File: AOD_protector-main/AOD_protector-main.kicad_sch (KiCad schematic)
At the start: 33 parts, among them IC1 MAX9141ESA+, J1 Input, J2 5V from source, J3 Output, J4 to fault handler, Q1 BSS316N, Q2 BSS316N, Q3 BSS316N, SW1 SW_Push, U1 REF35102QDBVR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

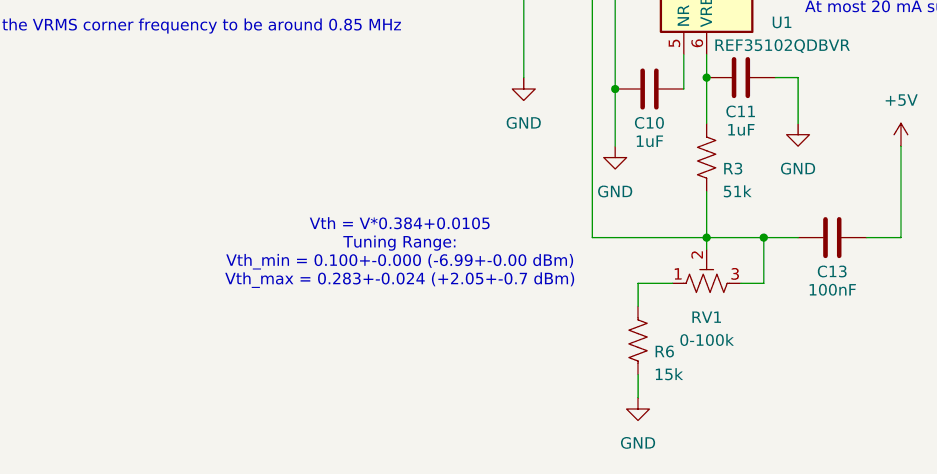
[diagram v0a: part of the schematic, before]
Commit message: Fixed a resistor value bug
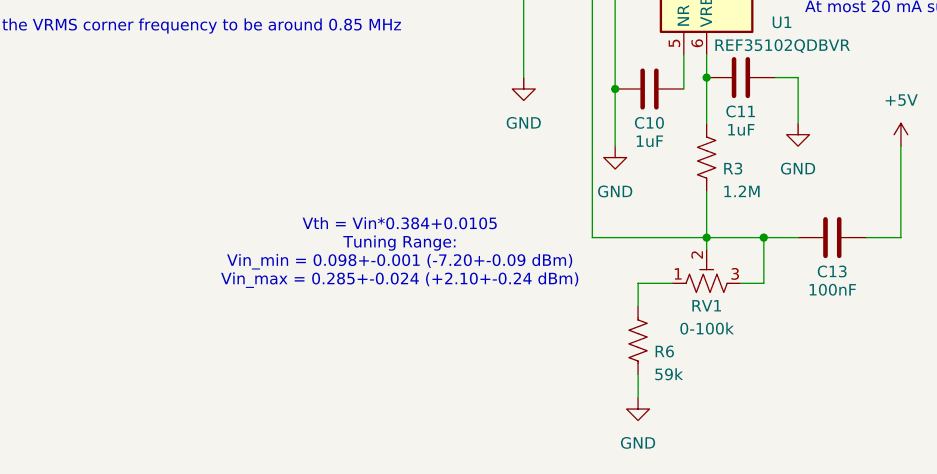
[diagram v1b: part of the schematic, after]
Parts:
- R3: value 51k -> 1.2M; footprint Resistor_SMD:R_0402_1005Metric -> Resistor_SMD:R_0603_1608Metric; JLCPCB Part C852828 -> C3933664; Part number RT0402BRD0751KL -> MCT0603MD1204BP500
- R6: value 15k -> 59k; JLCPCB Part C20627044 -> C852853; Part number TC02G1502BT -> RT0402BRD0759KL
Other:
- note added: "Vth = Vin*0.384+0.0105 Tuning Range: Vin_min = 0.098+-0.001 (-7.20+-0.09 dBm) Vin_max = 0.285+-0.024 (+2.10+-0.24 dBm)"
- note removed: "Vth = V*0.384+0.0105 Tuning Range: Vth_min = 0.100+-0.000 (-6.99+-0.00 dBm) Vth_max = 0.283+-0.024 (+2.05+-0.7 dBm)"
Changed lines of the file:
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@@
 		)
 	)
-	(text "Vth = V*0.384+0.0105\nTuning Range:\nVth_min = 0.100+-0.000 (-6.99+-0.00 dBm)\nVth_max = 0.283+-0.024 (+2.05+-0.7 dBm)"
+	(text "Vth = Vin*0.384+0.0105\nTuning Range:\nVin_min = 0.098+-0.001 (-7.20+-0.09 dBm)\nVin_max = 0.285+-0.024 (+2.10+-0.24 dBm)"
 		(exclude_from_sim no)
 		(at 118.364 157.988 0)
@@
 			)
 		)
-		(property "Value" "15k"
+		(property "Value" "59k"
 			(at 146.558 171.45 0)
 			(effects
@@
 			)
 		)
-		(property "Part number" "TC02G1502BT"
+		(property "Part number" "RT0402BRD0759KL"
 			(at 144.78 167.64 0)
 			(effects
@@
 			)
 		)
-		(property "JLCPCB Part" "C20627044"
+		(property "JLCPCB Part" "C852853"
 			(at 144.78 167.64 0)
 			(effects
@@
 		(on_board yes)
 		(dnp no)
-		(fields_autoplaced yes)
 		(property "Reference" "RV1"
-			(at 152.4 165.1 90)
+			(at 152.4 163.83 90)
 			(effects
 				(font
@@
 		)
 		(property "Value" "0-100k"
-			(at 152.4 167.64 90)
+			(at 152.4 166.37 90)
 			(effects
 				(font
@@
 			)
 		)
-		(property "Value" "51k"
+		(property "Value" "1.2M"
 			(at 154.178 151.13 0)
 			(effects
@@
 			)
 		)
-		(property "Footprint" "Resistor_SMD:R_0402_1005Metric"
+		(property "Footprint" "Resistor_SMD:R_0603_1608Metric"
 			(at 151.384 147.066 90)
 			(effects
@@
 			)
 		)
-		(property "Part number" "RT0402BRD0751KL"
+		(property "Part number" " MCT0603MD1204BP500"
 			(at 152.4 147.32 0)
 			(effects
@@
 			)
 		)
-		(property "JLCPCB Part" "C852828"
+		(property "JLCPCB Part" "C3933664"
 			(at 152.4 147.32 0)
 			(effects
